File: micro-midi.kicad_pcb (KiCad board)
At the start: 2 copper layers, 6 parts, among them J1 AudioJack3, J2 Conn_01x03_Male, U1 6N137

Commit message: first try placing components
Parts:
- added D2: LED, LED_SMD:LED_0805_2012Metric_Pad1.15x1.40mm_HandSolder, F.Cu at (101.1, 79.2)
- added D3: LED, LED_SMD:LED_0805_2012Metric_Pad1.15x1.40mm_HandSolder, F.Cu at (124.0, 83.3)
- added J3: AudioJack3, Connector_Audio:Jack_3.5mm_QingPu_WQP-PJ398SM_Vertical_CircularHoles, F.Cu at (81.3, 45.9)
- added R3: 470, Resistor_SMD:R_0805_2012Metric_Pad1.15x1.40mm_HandSolder, F.Cu at (105.2, 76.2)
- added R4: 470, Resistor_SMD:R_0805_2012Metric_Pad1.15x1.40mm_HandSolder, F.Cu at (124.0, 79.2)
- added R5: 220R, Resistor_SMD:R_0805_2012Metric_Pad1.15x1.40mm_HandSolder, F.Cu at (84.3, 63.0)
- added R6: 220R, Resistor_SMD:R_0805_2012Metric_Pad1.15x1.40mm_HandSolder, F.Cu at (102.6, 64.5)
- added U2: 6N137, Package_DIP:PowerIntegrations_SMD-8, F.Cu at (100.4, 49.8)
- D1: footprint Diode_THT:D_DO-35_SOD27_P7.62mm_Horizontal -> Diode_SMD:D_0805_2012Metric_Pad1.15x1.40mm_HandSolder
- J2: value Conn_01x03_Male -> Conn_01x04_Male; footprint Connector_PinHeader_2.54mm:PinHeader_1x03_P2.54mm_Vertical -> Connector_PinHeader_2.54mm:PinHeader_1x04_P2.54mm_Vertical
- R1: value 10K -> 220R; footprint Resistor_SMD:R_1206_3216Metric -> Resistor_SMD:R_0805_2012Metric_Pad1.15x1.40mm_HandSolder
- R2: value 220R -> 10K; footprint Resistor_SMD:R_1206_3216Metric -> Resistor_SMD:R_0805_2012Metric_Pad1.15x1.40mm_HandSolder
- U1: value 6N137 -> 74HC04; footprint Package_DIP:DIP-8_W7.62mm -> Package_SO:SOIC-14_3.9x8.7mm_P1.27mm
- moved D1 48.9 mm to (90.9, 73.2)
- moved R1 41.6 mm to (90.9, 78.7), turned to 180 degrees
- moved J2 39.2 mm to (136.7, 52.3)
- moved R2 16.7 mm to (112.3, 49.3), turned to 90 degrees
- moved U1 16.1 mm to (112.8, 75.7)
- moved J1 11.8 mm to (81.3, 70.1)
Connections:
- J1 pad S: Net-(J1-PadS) -> (no net)
- J2 pad 1: GND -> +5V
- J2 pad 3: +5V -> Net-(J2-Pad3)
- R1 pad 1: Net-(J2-Pad2) -> Net-(D1-Pad1)
- R1 pad 2: +5V -> Net-(J1-PadT)
- R2 pad 1: Net-(D1-Pad1) -> Net-(J2-Pad2)
- R2 pad 2: Net-(J1-PadT) -> +5V
- U1 pad 1: Net-(U1-Pad1) -> Net-(J2-Pad3)
- U1 pad 2: Net-(D1-Pad1) -> Net-(U1-Pad2)
- U1 pad 3: Net-(D1-Pad2) -> Net-(U1-Pad2)
- U1 pad 4: (no net) -> Net-(R5-Pad2)
- U1 pad 5: GND -> Net-(J2-Pad3)
- U1 pad 6: Net-(J2-Pad2) -> Net-(R3-Pad2)
- U1 pad 7: Net-(U1-Pad7) -> GND
- U1 pad 8: +5V -> Net-(R4-Pad2)
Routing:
- added copper zone on F.Cu, net GND
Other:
- board outline added: 72.4 x 45.7 mm

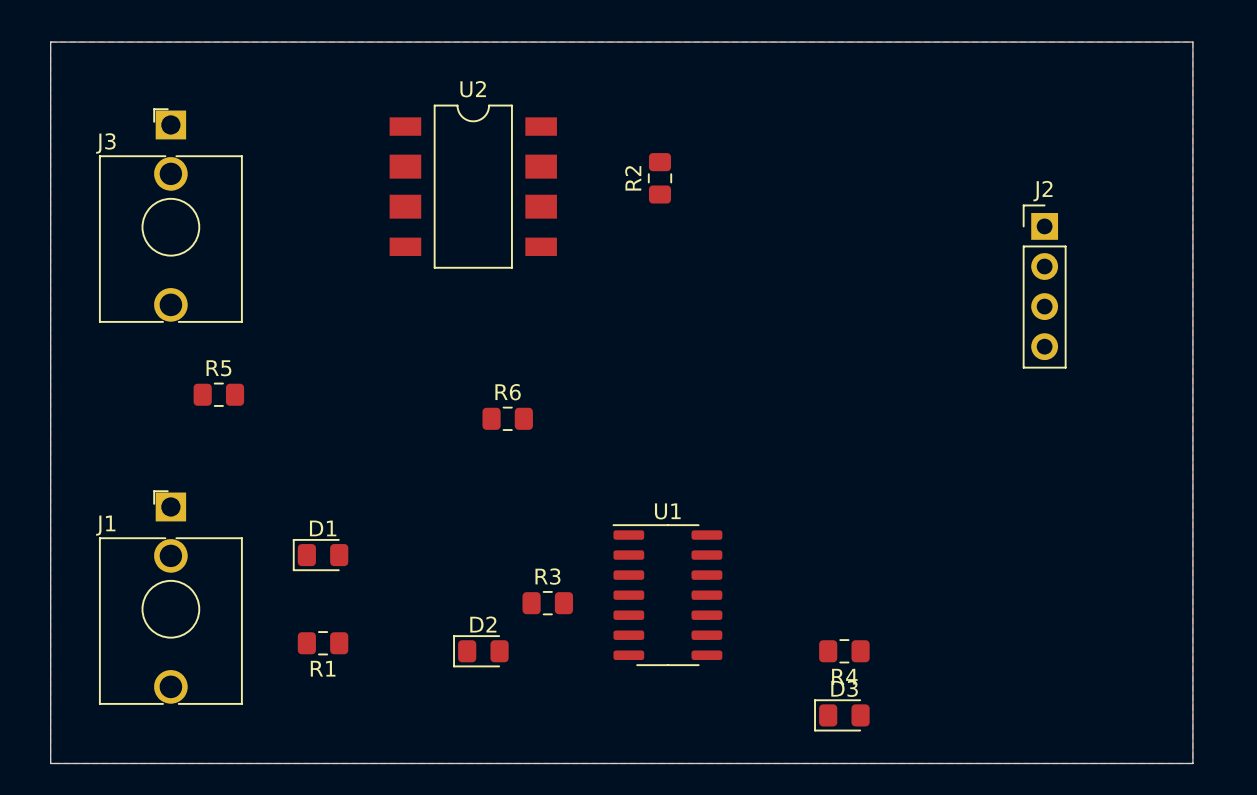
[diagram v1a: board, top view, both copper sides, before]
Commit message: some routing, rename pads on jacks to fix missing connection
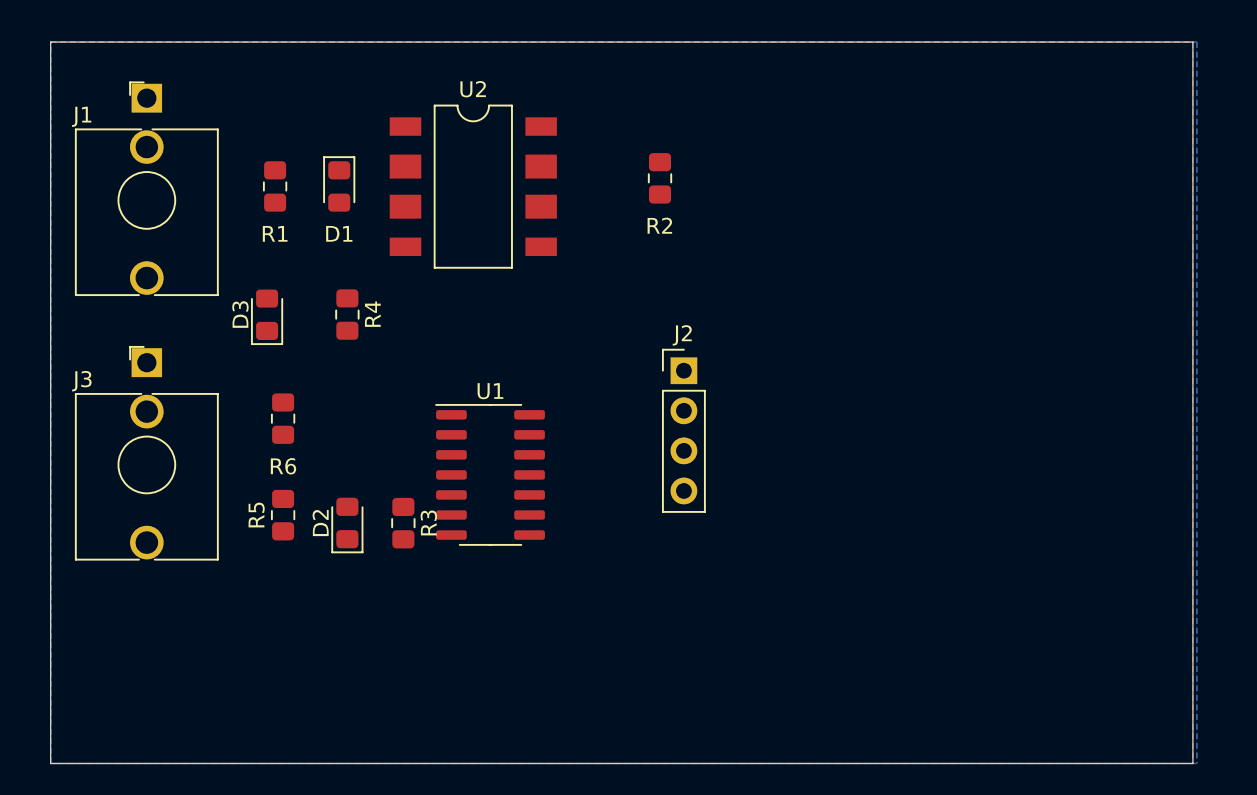
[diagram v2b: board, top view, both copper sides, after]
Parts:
- moved D3 44.5 mm to (87.4, 57.9), turned to 90 degrees
- moved R4 38.0 mm to (92.5, 57.9), turned to 270 degrees
- moved R1 29.1 mm to (87.9, 49.8), turned to 270 degrees
- moved J1 26.0 mm to (79.8, 44.2)
- moved J2 24.6 mm to (113.8, 61.5)
- moved D1 23.4 mm to (91.9, 49.8), turned to 270 degrees
- moved J3 15.1 mm to (79.8, 61.0)
- moved R6 14.2 mm to (88.4, 64.5), turned to 90 degrees
- moved U1 13.6 mm to (101.5, 68.1)
- moved D2 11.8 mm to (92.5, 71.1), turned to 90 degrees
- moved R3 10.5 mm to (96.0, 71.1), turned to 270 degrees
- moved R5 8.65 mm to (88.4, 70.6), turned to 90 degrees
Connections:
- R6 pad 1: (no net) -> Net-(J3-PadR)
- U1 pad 2: Net-(U1-Pad2) -> Net-(R3-Pad2)
- U1 pad 3: Net-(U1-Pad2) -> Net-(U1-Pad3)
- U1 pad 6: Net-(R3-Pad2) -> Net-(U1-Pad3)
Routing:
- added copper zone on B.Cu, net +5V

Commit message: some routing
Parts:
- J2: moved to B.Cu
- moved R3 10.7 mm to (88.0, 64.0), turned to 0 degrees
- moved D2 10.6 mm to (88.0, 61.5), turned to 180 degrees
- moved J2 7.90 mm to (106.0, 62.8), turned to 180 degrees
- moved R2 6.30 mm to (106.0, 48.7)
- moved R4 5.45 mm to (88.0, 54.8), turned to 0 degrees
- moved U1 5.09 mm to (97.0, 65.8)
- moved D1 3.92 mm to (88.0, 49.8), turned to 180 degrees
- moved J3 3.58 mm to (79.2, 64.5)
- moved U2 2.74 mm to (98.0, 48.6)
- moved R1 2.46 mm to (88.0, 52.2), turned to 180 degrees
- moved R6 2.28 mm to (88.0, 66.8), turned to 0 degrees
- moved J1 1.61 mm to (79.2, 42.7)
- moved R5 1.43 mm to (88.0, 69.2), turned to 0 degrees
- moved D3 0.93 mm to (88.0, 57.2), turned to 180 degrees
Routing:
- net Net-(D1-Pad2): track 0.00 -> 31.3 mm
- net Net-(J2-Pad2): track 0.00 -> 22.0 mm
- net Net-(J3-PadT): track 0.00 -> 10.5 mm
- net Net-(D1-Pad1): track 0.00 -> 8.61 mm
- net Net-(J1-PadT): track 0.00 -> 8.51 mm
- net +5V: track 0.00 -> 8.40 mm, vias 0 -> 2
- net Net-(J3-PadR): track 0.00 -> 8.05 mm
- net Net-(D3-Pad2): track 0.00 -> 2.50 mm
- net Net-(D2-Pad2): track 0.00 -> 2.50 mm
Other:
- board text added: "MIDI in"
- board text added: "MIDI out"

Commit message: fix board edge
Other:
- board size 72.4 x 45.7 mm -> 36 x 39 mm
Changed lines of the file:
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@@
   (general
     (thickness 1.6)
-    (drawings 6)
+    (drawings 10)
     (tracks 35)
     (zones 0)
@@
   (page A4)
   (layers
-    (0 F.Cu signal)
+    (0 F.Cu signal hide)
     (31 B.Cu signal hide)
     (32 B.Adhes user)
@@
     )
   )
+  (gr_line (start 73 78) (end 73 41) (layer Edge.Cuts) (width 0.05))
+  (gr_line (start 108 79) (end 74 79) (layer Edge.Cuts) (width 0.05))
+  (gr_line (start 109 41) (end 109 78) (layer Edge.Cuts) (width 0.05))
+  (gr_line (start 74 40) (end 108 40) (layer Edge.Cuts) (width 0.05))
+  (gr_arc (start 108 41) (end 109 41) (angle -90) (layer Edge.Cuts) (width 0.05))
+  (gr_arc (start 108 78) (end 108 79) (angle -90) (layer Edge.Cuts) (width 0.05))
+  (gr_arc (start 74 78) (end 73 78) (angle -90) (layer Edge.Cuts) (width 0.05))
+  (gr_arc (start 74 41) (end 74 40) (angle -90) (layer Edge.Cuts) (width 0.05))
   (gr_text "MIDI out" (at 78.75 61.75) (layer F.SilkS)
     (effects (font (size 1.5 1.5) (thickness 0.3)))
@@
     (effects (font (size 1.5 1.5) (thickness 0.3)))
   )
-  (gr_line (start 73.66 86.36) (end 73.66 40.64) (layer Edge.Cuts) (width 0.05))
-  (gr_line (start 146.05 86.36) (end 73.66 86.36) (layer Edge.Cuts) (width 0.05))
-  (gr_line (start 146.05 40.64) (end 146.05 86.36) (layer Edge.Cuts) (width 0.05))
-  (gr_line (start 73.66 40.64) (end 146.05 40.64) (layer Edge.Cuts) (width 0.05))
   (segment (start 79.248 45.772) (end 83.226 49.75) (width 0.5) (layer F.Cu) (net 1))
   (segment (start 83.226 49.75) (end 87 49.75) (width 0.5) (layer F.Cu) (net 1))
@@
     (connect_pads (clearance 0.508))
     (min_thickness 0.254)
-    (fill yes (arc_segments 32) (thermal_gap 0.508) (thermal_bridge_width 0.508))
+    (fill (arc_segments 32) (thermal_gap 0.508) (thermal_bridge_width 0.508))
     (polygon
       (pts
@@
     (connect_pads (clearance 0.508))
     (min_thickness 0.254)
-    (fill yes (arc_segments 32) (thermal_gap 0.508) (thermal_bridge_width 0.508))
+    (fill (arc_segments 32) (thermal_gap 0.508) (thermal_bridge_width 0.508))
     (polygon
       (pts
